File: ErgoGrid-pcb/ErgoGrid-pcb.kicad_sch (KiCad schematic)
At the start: 26 parts, among them J1 MCU_inside, J2 MCU_outside

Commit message: pcb: add key and RGB grids to schematic
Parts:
- added J3: mcu_3pin, symbol Conn_01x05:Conn_01x05
- renumbered JP3 to JP1, JP6 to JP10, JP9 to JP11, JP10 to JP12, JP15 to JP13, JP16 to JP14, JP19 to JP15, JP20 to JP16, JP23 to JP17, JP24 to JP18, JP13 to JP19, JP4 to JP2, JP14 to JP20, JP17 to JP21, JP18 to JP22, JP21 to JP23, JP22 to JP24, JP7 to JP3, JP8 to JP4, JP11 to JP5, JP12 to JP6, JP1 to JP7, JP2 to JP8, JP5 to JP9
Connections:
- new net encA: J3.1 (Pin_1), J3.5 (Pin_5)
- new net encB: J3.2 (Pin_2), J3.4 (Pin_4)

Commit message: pcb: almost done with schematic
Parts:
- added J4: AudioJack4, symbol AudioJack4:AudioJack4
- added J5: USB_5V, symbol Conn_01x01:Conn_01x01
- added J6: OLED, symbol Conn_01x04:Conn_01x04
- added J7: Battery, symbol Conn_01x02:Conn_01x02
- added J8: Joystick_L, symbol Conn_01x05_MountingPin:Conn_01x05_MountingPin
- added J9: Joystick_R, symbol Conn_01x05_MountingPin:Conn_01x05_MountingPin
- added JP27: OLED_SDA_L, symbol Jumper_2_Small_Open:Jumper_2_Small_Open
- added JP28: OLED_SCL_L, symbol Jumper_2_Small_Open:Jumper_2_Small_Open
- added JP29: OLED_VCC_L, symbol Jumper_2_Small_Open:Jumper_2_Small_Open
- added JP30: OLED_GND_L, symbol Jumper_2_Small_Open:Jumper_2_Small_Open
- added JP31: OLED_GND_R, symbol Jumper_2_Small_Open:Jumper_2_Small_Open
- added JP32: OLED_VCC_R, symbol Jumper_2_Small_Open:Jumper_2_Small_Open
- added JP33: OLED_SCL_R, symbol Jumper_2_Small_Open:Jumper_2_Small_Open
- added JP34: OLED_SDA_R, symbol Jumper_2_Small_Open:Jumper_2_Small_Open
- added JP35: GND_bat_L, symbol Jumper_2_Small_Open:Jumper_2_Small_Open
- added JP36: GND_bat_R, symbol Jumper_2_Small_Open:Jumper_2_Small_Open
- added JP37: Plus_bat_L, symbol Jumper_2_Small_Open:Jumper_2_Small_Open
- added JP38: Plus_bat_R, symbol Jumper_2_Small_Open:Jumper_2_Small_Open
- added SW23: SW_Push, symbol SW_Push:SW_Push
- added SW24, SW25: SW_SPDT, symbol SW_SPDT:SW_SPDT
- J3: value mcu_3pin -> MCU_3pin
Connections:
- net +BATT: now also SW24.3 (C), SW25.1 (A)
- net AIN_0: now also J8.2 (Pin_2), J9.2 (Pin_2)
- net AIN_1: now also J8.5 (Pin_5), J9.5 (Pin_5)
- net GND: now also J4.T, J8.4 (Pin_4), J8.MP (MountPin), J9.4 (Pin_4), J9.MP (MountPin), JP30.2 (B), JP31.2 (B), JP35.1 (A), JP36.2 (B), SW23.1
- net RST: now also SW23.2
- net RX: now also J4.R2
- net SCL: now also JP28.2 (B), JP33.2 (B)
- net SDA: now also JP27.2 (B), JP34.2 (B)
- net TX: now also J4.R1
- net VCC: now also J8.1 (Pin_1), J9.1 (Pin_1), JP29.2 (B), JP32.2 (B)
- net JoyBtn: now reaches J3.3 (Pin_3)
- net JoyBtn: now also J8.3 (Pin_3), J9.3 (Pin_3)
- net encA renamed EncA
- net encB renamed EncB
- new net: J7.1 (Pin_1), JP35.2 (B), JP38.1 (A)
- new net: J7.2 (Pin_2), JP36.1 (A), JP37.1 (A)
- new net: J6.4 (Pin_4), JP30.1 (A), JP34.1 (A)
- new net: J6.1 (Pin_1), JP27.1 (A), JP31.1 (A)
- new net: J6.2 (Pin_2), JP28.1 (A), JP32.1 (A)
- new net: J6.3 (Pin_3), JP29.1 (A), JP33.1 (A)
- new net: JP37.2 (B), JP38.2 (B), SW24.2 (B), SW25.2 (B)
- new net +5V: J4.S, J5.1 (Pin_1)
- no-connect marks 0 -> 2
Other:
- note added: "- +"
- note added: "BATTERY"
- note added: "DISPLAY"
- note added: "JOYSTICK"
- note added: "MCU MODULE"
- note added: "POWER FLAGS"
- note added: "SPLIT HALF CONNECTION"
- moved on the sheet: J1, J2, J3, JP1, JP10, JP11, JP12, JP13, JP14, JP15, JP16, JP17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

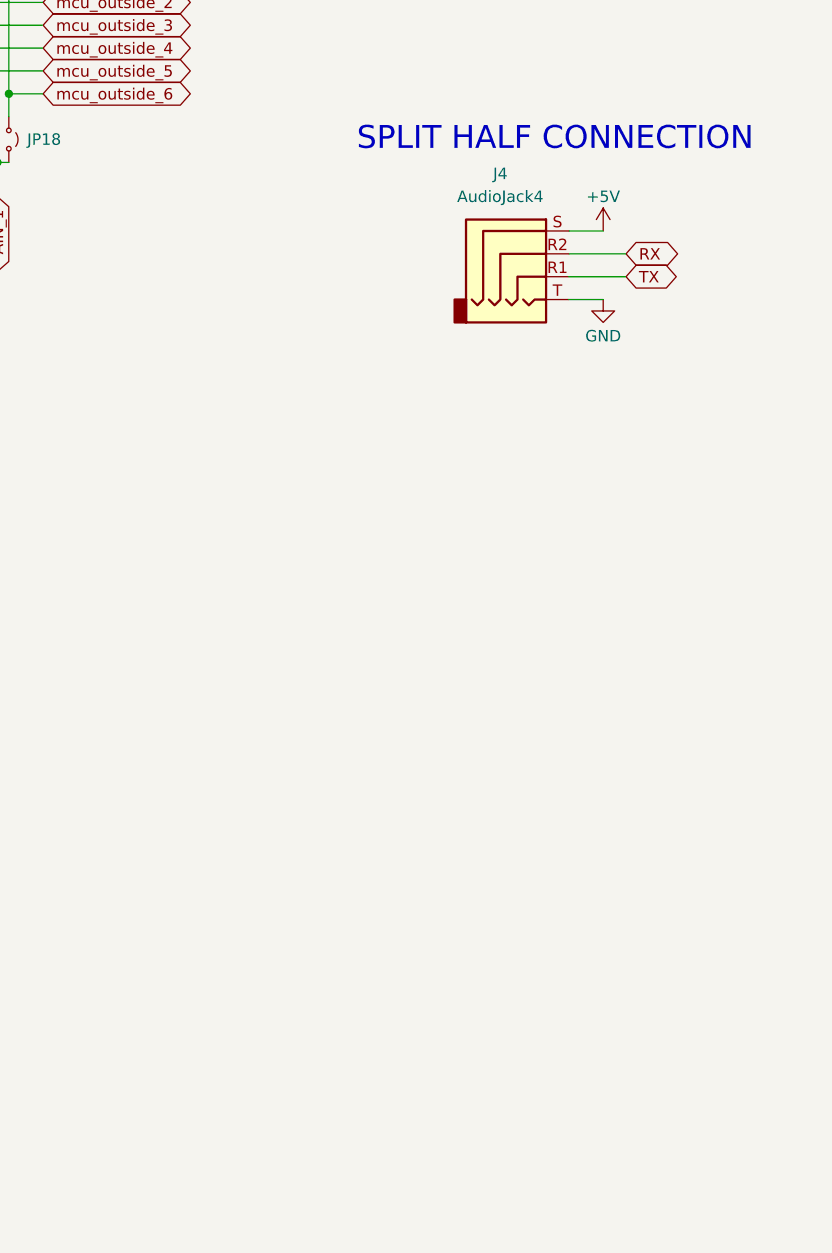
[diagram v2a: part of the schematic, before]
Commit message: pcb: add piezo haptic
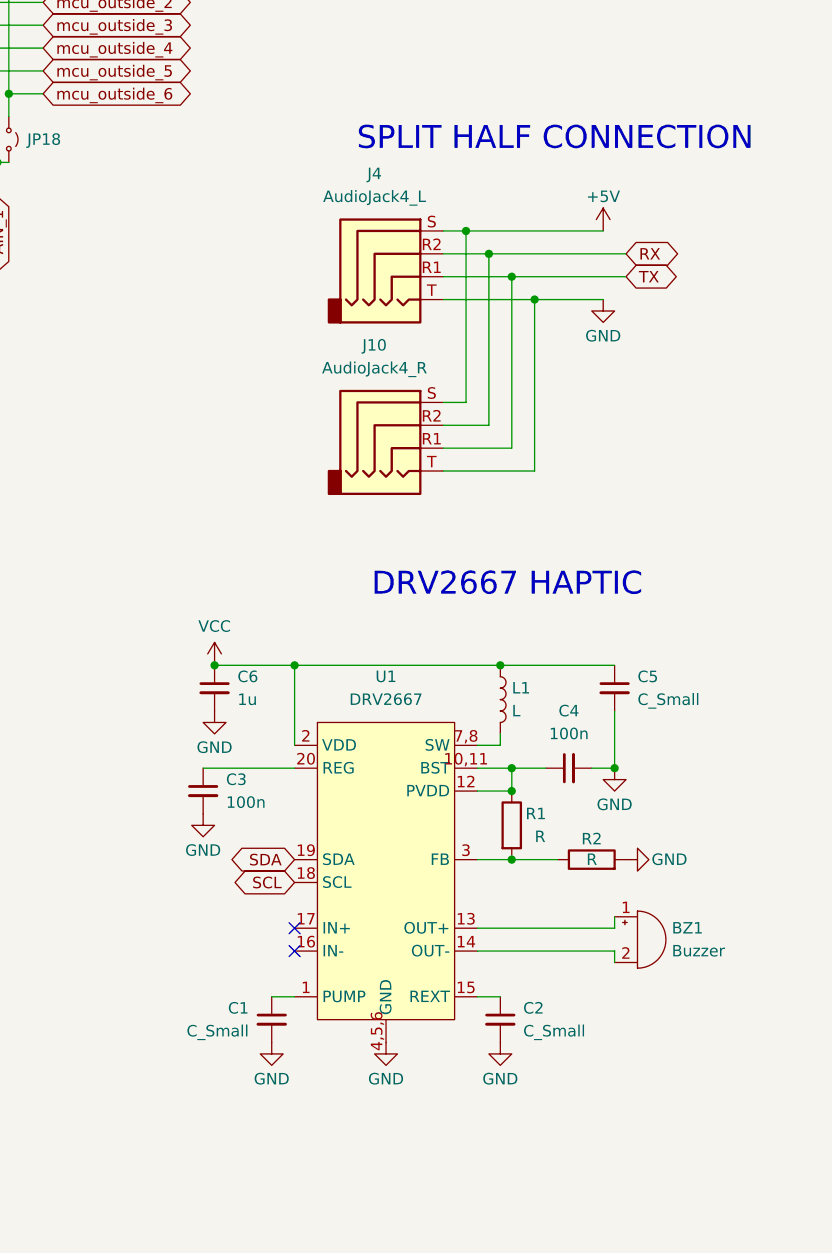
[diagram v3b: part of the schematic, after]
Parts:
- added BZ1: Buzzer, symbol Buzzer:Buzzer
- added C1, C2, C5: C_Small, symbol C_Small:C_Small
- added C3, C4: 100n, symbol C_Small:C_Small
- added C6: 1u, symbol C_Small:C_Small
- added J10: AudioJack4_R, symbol AudioJack4:AudioJack4
- added L1: L, symbol L:L
- added R1, R2: R, symbol R:R
- added U1: DRV2667, Package_DFN_QFN:QFN-20-1EP_4x4mm_P0.5mm_EP2.7x2.7mm_ThermalVias, symbol ErgoGrid_SymLib:DRV2667
- J4: value AudioJack4 -> AudioJack4_L
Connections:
- net +5V: now also J10.S
- net GND: now also C1.2, C2.2, C3.2, C4.2, C5.2, C6.2, J10.T, R2.2, U1.4,5,6 (GND)
- net RX: now also J10.R2
- net SCL: now also U1.18 (SCL)
- net SDA: now also U1.19 (SDA)
- net TX: now also J10.R1
- net VCC: now also C5.1, C6.1, L1.1, U1.2 (VDD)
- new net: C1.1, U1.1 (PUMP)
- new net: L1.2, U1.7,8 (SW)
- new net: C4.1, R1.1, U1.10,11 (BST), U1.12 (PVDD)
- new net: BZ1.1 (+), U1.13 (OUT+)
- new net: BZ1.2 (-), U1.14 (OUT-)
- new net: C2.1, U1.15 (REXT)
- new net: C3.1, U1.20 (REG)
- new net: R1.2, R2.1, U1.3 (FB)
- no-connect marks 2 -> 4
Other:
- note added: "DRV2667 HAPTIC"
- moved on the sheet: J4

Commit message: pcb: complete schematic
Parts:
- removed C2: C_Small, symbol C_Small:C_Small
- added R3: 142k, Resistor_SMD:R_0603_1608Metric, symbol R:R
- added S2: RST_R, symbol SW_Push:SW_Push
- C1: renamed from C6; footprint (none) -> Capacitor_SMD:C_0805_2012Metric
- C2: renamed from C5; value C_Small -> 10u; footprint (none) -> Capacitor_SMD:C_1206_3216Metric
- C3: renamed from C4; footprint (none) -> Capacitor_SMD:C_0805_2012Metric
- C4: renamed from C3; footprint (none) -> Capacitor_SMD:C_0805_2012Metric
- C5: renamed from C1; value C_Small -> 100n 100V; footprint (none) -> Capacitor_SMD:C_0805_2012Metric
- JP1, JP10, JP11, JP12, JP13, JP14, JP15, JP16, JP17, JP18, JP19, JP2, JP20, JP21, JP22, JP23, JP24, JP3, JP31, JP4, JP5, JP6, JP7, JP8, JP9: footprint (none) -> Jumper:SolderJumper-2_P1.3mm_Open_TrianglePad1.0x1.5mm
- JP25: renamed from JP27; footprint (none) -> Jumper:SolderJumper-2_P1.3mm_Open_TrianglePad1.0x1.5mm
- JP26: renamed from JP28; footprint (none) -> Jumper:SolderJumper-2_P1.3mm_Open_TrianglePad1.0x1.5mm
- JP27: renamed from JP37; footprint (none) -> Jumper:SolderJumper-2_P1.3mm_Open_TrianglePad1.0x1.5mm
- JP28: renamed from JP29; footprint (none) -> Jumper:SolderJumper-2_P1.3mm_Open_TrianglePad1.0x1.5mm
- JP29: renamed from JP30; footprint (none) -> Jumper:SolderJumper-2_P1.3mm_Open_TrianglePad1.0x1.5mm
- JP30: renamed from JP38; footprint (none) -> Jumper:SolderJumper-2_P1.3mm_Open_TrianglePad1.0x1.5mm
- JP32: renamed from JP35; footprint (none) -> Jumper:SolderJumper-2_P1.3mm_Open_TrianglePad1.0x1.5mm
- JP33: renamed from JP36; footprint (none) -> Jumper:SolderJumper-2_P1.3mm_Open_TrianglePad1.0x1.5mm
- JP34: renamed from JP32; footprint (none) -> Jumper:SolderJumper-2_P1.3mm_Open_TrianglePad1.0x1.5mm
- JP35: renamed from JP33; footprint (none) -> Jumper:SolderJumper-2_P1.3mm_Open_TrianglePad1.0x1.5mm
- JP36: renamed from JP34; footprint (none) -> Jumper:SolderJumper-2_P1.3mm_Open_TrianglePad1.0x1.5mm
- L1: value L -> 3u3
- R1: value R -> 500k; footprint (none) -> Resistor_SMD:R_0603_1608Metric
- R2: value R -> 20k; footprint (none) -> Resistor_SMD:R_0603_1608Metric
- S1: renamed from SW23; value SW_Push -> RST_L
- S3: renamed from SW24; value SW_SPDT -> BAT_L
- S4: renamed from SW25; value SW_SPDT -> BAT_R
- renumbered J9 to J10, J5 to J3, J10 to J5, J3 to J6, J6 to J8, J8 to J9
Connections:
- net +5V: now also C1.1, C2.1, L1.1, U1.2 (VDD)
- net GND: now also R3.2, S2.1
- net RST: now also S2.2
- net VCC: no longer C1.1, C2.1, L1.1, U1.2 (VDD)
- net at U1.15 (REXT): now also R3.1
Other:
- note added: "29.3V peak"
- note added: "Boost limit 100mA"
- moved on the sheet: BZ1, C1, C2, C3, C4, C5, L1, R1, R2, U1

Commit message: pcb: assigned some footprints
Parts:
- J1, J2: footprint (none) -> Connector_PinSocket_2.54mm:PinSocket_1x12_P2.54mm_Vertical
- J10, J9: footprint (none) -> Connector_FFC-FPC:Amphenol_F32Q-1A7x1-11005_1x05-1MP_P0.5mm_Horizontal
- J3: footprint (none) -> Connector_Pin:Pin_D0.7mm_L6.5mm_W1.8mm_FlatFork
- J7: footprint (none) -> Connector_JST:JST_PH_S2B-PH-K_1x02_P2.00mm_Horizontal
- J8: footprint (none) -> Connector_PinSocket_2.54mm:PinSocket_1x04_P2.54mm_Vertical
- S1, S2: footprint (none) -> Button_Switch_SMD:SW_SPST_EVQP7C
- S3, S4: footprint (none) -> Button_Switch_SMD:SW_SPDT_PCM12
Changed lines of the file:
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@@
 			)
 		)
-		(property "Footprint" ""
+		(property "Footprint" "Connector_JST:JST_PH_S2B-PH-K_1x02_P2.00mm_Horizontal"
 			(at 82.55 165.1 0)
 			(hide yes)
@@
 			)
 		)
-		(property "Footprint" ""
+		(property "Footprint" "Connector_PinSocket_2.54mm:PinSocket_1x12_P2.54mm_Vertical"
 			(at 45.72 43.18 0)
 			(hide yes)
@@
 			)
 		)
-		(property "Footprint" ""
+		(property "Footprint" "Connector_Pin:Pin_D0.7mm_L6.5mm_W1.8mm_FlatFork"
 			(at 53.34 52.07 0)
 			(hide yes)
@@
 			)
 		)
-		(property "Footprint" ""
+		(property "Footprint" "Connector_PinSocket_2.54mm:PinSocket_1x04_P2.54mm_Vertical"
 			(at 125.73 173.99 0)
 			(hide yes)
@@
 			)
 		)
-		(property "Footprint" ""
+		(property "Footprint" "Button_Switch_SMD:SW_SPDT_PCM12"
 			(at 97.79 172.72 0)
 			(hide yes)
@@
 			)
 		)
-		(property "Footprint" ""
+		(property "Footprint" "Connector_FFC-FPC:Amphenol_F32Q-1A7x1-11005_1x05-1MP_P0.5mm_Horizontal"
 			(at 55.88 179.07 0)
 			(hide yes)
@@
 			)
 		)
-		(property "Footprint" ""
+		(property "Footprint" "Button_Switch_SMD:SW_SPST_EVQP7C"
 			(at 72.39 106.68 0)
 			(hide yes)
@@
 			)
 		)
-		(property "Footprint" ""
+		(property "Footprint" "Connector_FFC-FPC:Amphenol_F32Q-1A7x1-11005_1x05-1MP_P0.5mm_Horizontal"
 			(at 21.59 179.07 0)
 			(hide yes)
@@
 			)
 		)
-		(property "Footprint" ""
+		(property "Footprint" "Button_Switch_SMD:SW_SPST_EVQP7C"
 			(at 72.39 90.17 0)
 			(hide yes)
@@
 			)
 		)
-		(property "Footprint" ""
+		(property "Footprint" "Button_Switch_SMD:SW_SPDT_PCM12"
 			(at 97.79 187.96 0)
 			(hide yes)
@@
 			)
 		)
-		(property "Footprint" ""
+		(property "Footprint" "Connector_PinSocket_2.54mm:PinSocket_1x12_P2.54mm_Vertical"
 			(at 62.23 43.18 0)
 			(hide yes)

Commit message: pcb: footprint assignment completed
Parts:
- BZ1: footprint (none) -> ErgoGrid:PiezoDisc_15mm_12mm
- J4, J5: footprint (none) -> Connector_Audio:Jack_3.5mm_PJ320D_Horizontal
- J6: footprint (none) -> ErgoGrid:ProMicro_3pin
- L1: footprint (none) -> Inductor_SMD:L_APV_APH0518
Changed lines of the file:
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@@
 			)
 		)
-		(property "Footprint" ""
+		(property "Footprint" "Inductor_SMD:L_APV_APH0518"
 			(at 246.38 118.11 0)
 			(hide yes)
@@
 			)
 		)
-		(property "Footprint" ""
+		(property "Footprint" "ErgoGrid:ProMicro_3pin"
 			(at 25.4 93.98 0)
 			(hide yes)
@@
 			)
 		)
-		(property "Footprint" ""
+		(property "Footprint" "Connector_Audio:Jack_3.5mm_PJ320D_Horizontal"
 			(at 234.95 90.17 0)
 			(hide yes)
@@
 			)
 		)
-		(property "Footprint" ""
+		(property "Footprint" "ErgoGrid:PiezoDisc_15mm_12mm"
 			(at 260.985 142.24 90)
 			(hide yes)
@@
 			)
 		)
-		(property "Footprint" ""
+		(property "Footprint" "Connector_Audio:Jack_3.5mm_PJ320D_Horizontal"
 			(at 234.95 71.12 0)
 			(hide yes)

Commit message: pcb: fix errors and warnings
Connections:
- net GND: now also U1.21 (PAD), U1.4 (GND), U1.5 (GND), U1.6 (GND); no longer U1.4,5,6 (GND)
- net at L1.2: now also U1.7 (SW), U1.8 (SW); no longer U1.7,8 (SW)
- net at C3.1, R1.1, U1.12 (PVDD): now also U1.10 (BST), U1.11 (BST); no longer U1.10,11 (BST)
- no-connect marks 4 -> 5
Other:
- moved on the sheet: C1, C4, C5
